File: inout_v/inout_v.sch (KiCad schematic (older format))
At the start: 1 part, among them P1 DIN_41612_128P

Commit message: Power net updates for Counter Cell I+II and Inout V
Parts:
- added U22001, U22004, U22005, U22007, U22010, U22012, U22015, U22017, U22018, U22019, U22021, U22026, U22029, U22032, U22034, U22036, U22038, U22039, U22040, U22042, U22043, U22045, U22047, U22049, U22050, U22052, U22053, U22054, U22058, U22059, U22061, U22062, U22064, U22065, U22067: 74HC02, symbol 74HC02
- added U22002, U22006, U22009, U22011, U22013, U22016, U22022, U22024, U22025, U22027, U22033, U22037, U22041, U22044, U22048, U22051, U22055, U22060, U22063, U22066, U22068, U22130: 74HC27, symbol 74HC27
- added U22003, U22008, U22014, U22020, U22023, U22131: 74HC04, symbol 74HC04
- added U22028, U22057: 74LVC07, symbol 74LVC07
- added U22035, U22046, U22056: 74HC4002, symbol 74HC4002
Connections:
- net labels added: +4VDC, +4VSW
- net labels removed: VCC
- wire segments 299 -> 320

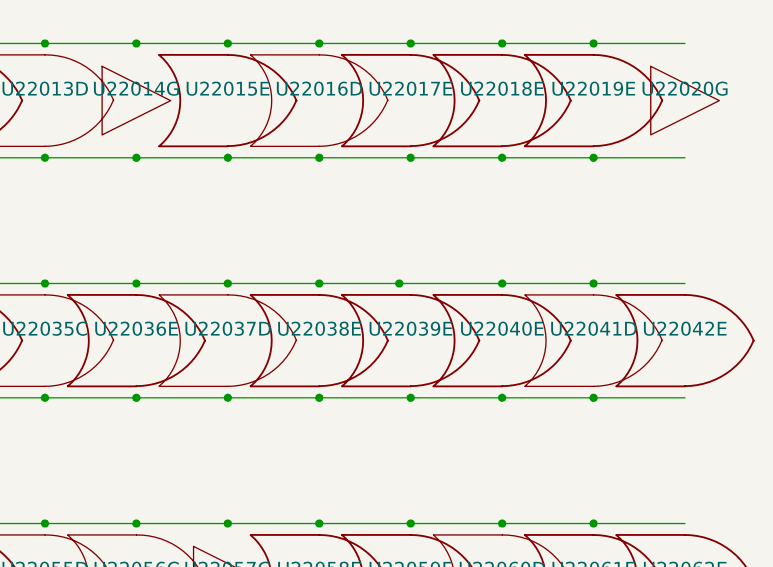
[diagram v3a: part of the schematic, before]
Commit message: Added the CH77 alarm box (restart monitor) and switched most (all?) monitor outputs over to open drain, largely using new 74LVC06 parts (which are used *only* for monitor outputs)
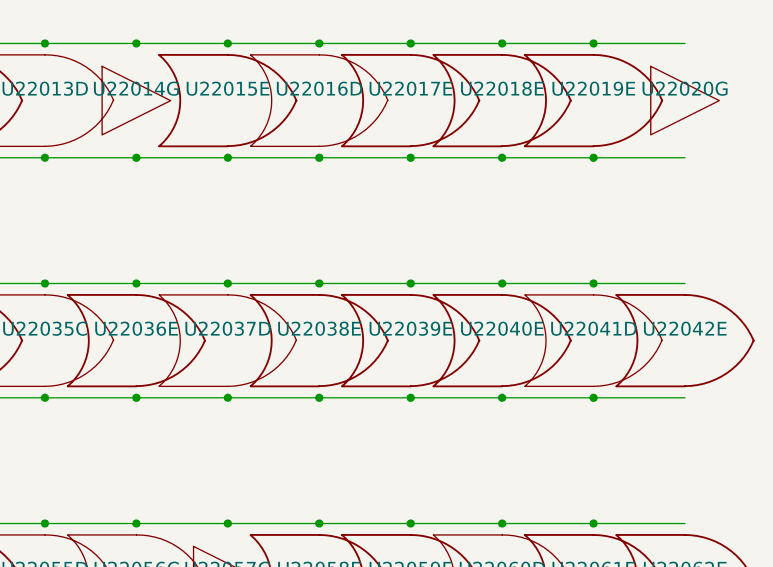
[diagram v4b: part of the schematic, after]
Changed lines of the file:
@@
 LIBS:contrib
 LIBS:valves
-LIBS:inout_v-cache
 EELAYER 25 0
 EELAYER END
@@
 Connection ~ 13900 7150
 Connection ~ 13500 7150
-Connection ~ 13050 7150
 Connection ~ 12700 7150
 Connection ~ 12300 7150
@@
 Connection ~ 10500 9250
 Connection ~ 10500 9750
+Connection ~ 13100 7150
 $EndSCHEMATC

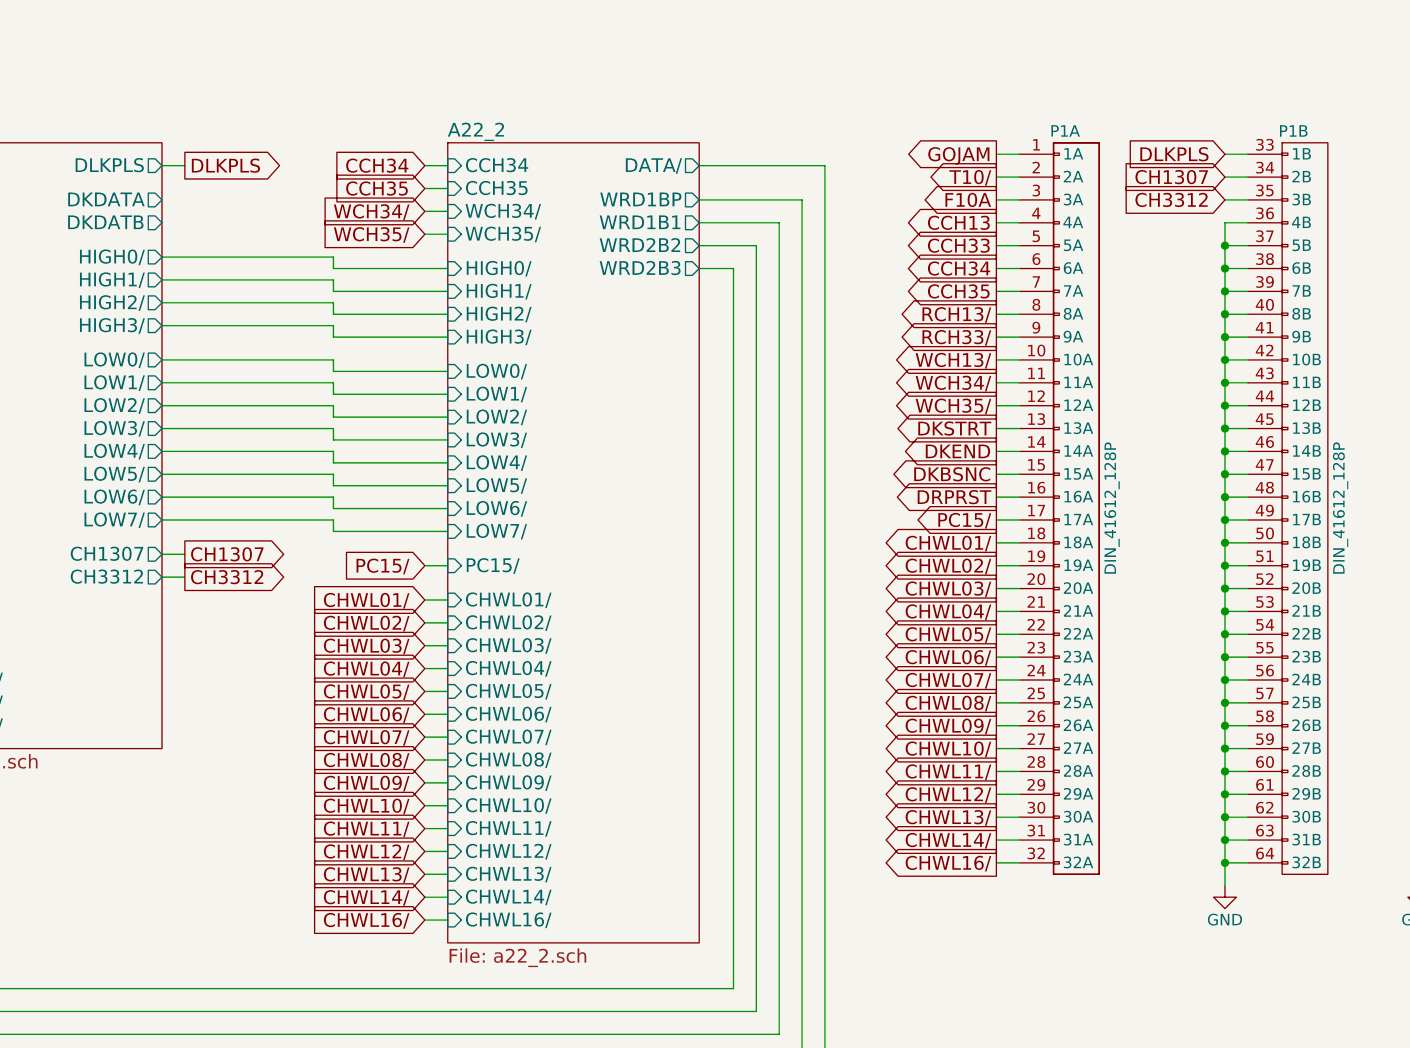
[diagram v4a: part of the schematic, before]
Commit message: Broke out the signals needed for downlink
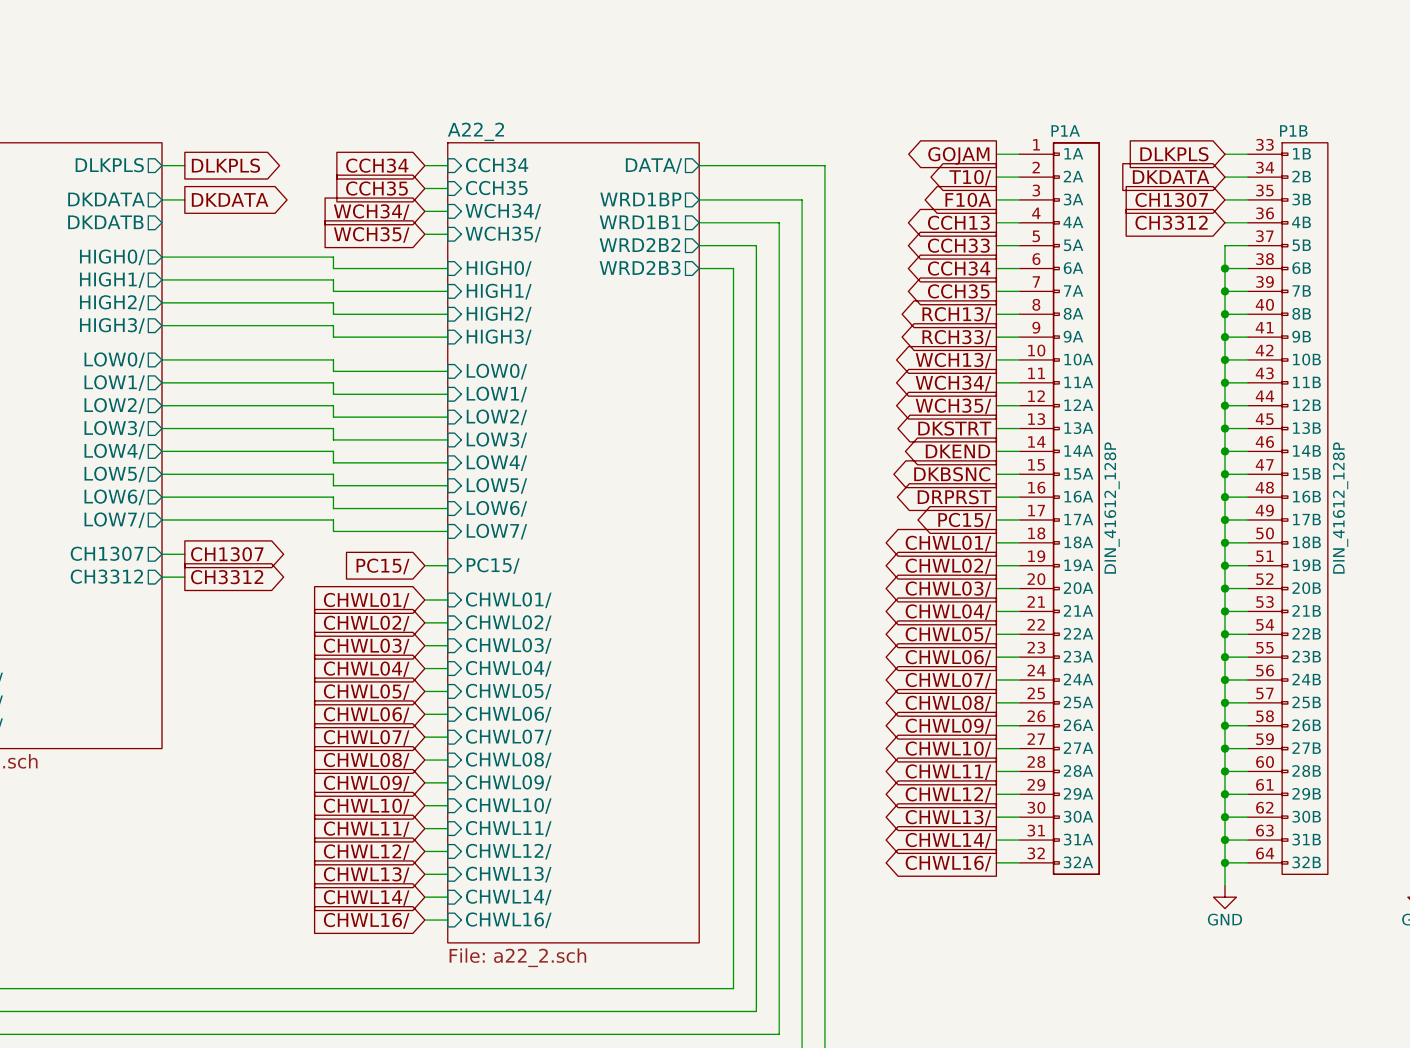
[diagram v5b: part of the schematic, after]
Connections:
- net labels added: DKDATA
- wire segments 320 -> 321
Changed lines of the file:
@@
 LIBS:contrib
 LIBS:valves
-EELAYER 25 0
+LIBS:inout_v-cache
+EELAYER 26 0
 EELAYER END
 $Descr A2 23386 16535
@@
 $EndComp
 Wire Wire Line
-	7400 1550 7500 1550
-Wire Wire Line
 	7400 1650 7500 1650
-Connection ~ 7400 1650
 Wire Wire Line
 	7400 1750 7500 1750
@@
 	7400 4350 7500 4350
 Connection ~ 7400 4350
-Wire Wire Line
-	7400 1550 7400 4450
 $Comp
 L GND #PWR01
@@
 DLKPLS
 Wire Wire Line
-	7500 1350 7400 1350
-Text GLabel 7400 1350 0    60   Input ~ 0
-CH1307
-Wire Wire Line
 	7500 1450 7400 1450
 Text GLabel 7400 1450 0    60   Input ~ 0
+CH1307
+Wire Wire Line
+	7500 1550 7400 1550
+Text GLabel 7400 1550 0    60   Input ~ 0
 CH3312
 $Comp
@@
 Connection ~ 10500 9750
 Connection ~ 13100 7150
+Wire Wire Line
+	2750 1450 2850 1450
+Text GLabel 2850 1450 2    60   Output ~ 0
+DKDATA
+Wire Wire Line
+	7400 4450 7400 1650
+Wire Wire Line
+	7500 1350 7400 1350
+Text GLabel 7400 1350 0    60   Input ~ 0
+DKDATA
 $EndSCHEMATC
